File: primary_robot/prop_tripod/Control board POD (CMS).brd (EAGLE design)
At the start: 100.7 x 157 mm, 94 parts, among them IC3 NE555D, Q1 MOSFET-NCHANNELD2PAK, Q2 MOSFET-NCHANNELD2PAK, Q3 MOSFET-NCHANNELD2PAK, Q4 MOSFET-NCHANNELD2PAK

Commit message: [prop_tripod] Updates to pre-Rev2
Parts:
- removed C10: 120nF, resistor:A/3216-18W
- removed C9: 330nF, rcl:A/3216-18R
- removed MC78M05ABT: MC78M05ABDT, linear:DPACK_3
- added R17: 1k, SparkFun-Passives:0603-RES
- moved R40 9.27 mm to (10.8, 124.5)
- moved D14 7.23 mm to (12.1, 97.8)
- moved C4 7.08 mm to (17.6, 100.2)
- moved D7 6.49 mm to (14.5, 101.0)
- moved LED1 5.74 mm to (-14.1, 104.1)
- moved Q1 5.72 mm to (-5.35, 104.1)
- moved Q2 5.72 mm to (-5.35, 131.0)
- moved R1 5.21 mm to (-14.1, 96.5)
- moved C7 4.59 mm to (-15.7, 113.0)
- moved BAT 4.57 mm to (-21.6, 100.3)
- moved TPS2 4.57 mm to (-16.6, 136.1)
- moved C8 3.70 mm to (-20.1, 111.3)
- moved C1 3.69 mm to (-21.8, 119.3)
- moved R41 3.68 mm to (13.1, 108.3), turned to 270 degrees
- moved M 3.05 mm to (-21.5, 126.4)
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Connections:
- removed net 5V_PWR: C10.+, MC78M05ABT.3
- net 12V_BAT: now also R17.2, TPS1.C; no longer C9.+, MC78M05ABT.1, TPS1.A
- net GND_PWR: now also TPS1.A, TPS2.A, TPS3.A; no longer C10.-, C9.-, MC78M05ABT.4, TPS1.C, TPS2.C, TPS3.C
- net N$11: now also TPS2.C; no longer TPS2.A
- net N$3: now also TPS3.C; no longer TPS3.A
- net N$64: now also R17.1
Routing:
- net N$3: track 98.5 -> 131.3 mm
- net 5V_PWR: track 10.5 -> 0.00 mm
- net 12V_BAT: track 316.1 -> 306.3 mm, vias 4 -> 5
- net GATE_Q3: track 23.2 -> 15.1 mm
- net N$2: track 66.3 -> 58.4 mm
- net N$11: track 71.8 -> 78.2 mm
- net GND_CMD: track 306.9 -> 312.9 mm
- net BSTRP: track 61.9 -> 56.2 mm
- net N$64: track 15.8 -> 18.7 mm
- net GND_PWR: track 445.4 -> 442.5 mm, vias 9 -> 10
- net DIR_POD3_LPC: track 14.2 -> 16.7 mm
- net DIR_POD1_LPC: track 11.5 -> 14.0 mm
- net PWM_POD2_LPC: track 14.8 -> 17.3 mm
- net PWM_POD1_LPC: track 11.2 -> 13.8 mm
- net PWM_POD3_LPC: track 16.0 -> 18.6 mm
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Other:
- board text added: "Carte POD rev2"
- board text removed: "Carte POD rev1"

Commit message: [prop-tripod] Update the footprint of the LPC, increase the readability of some name on the board
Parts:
- moved CON_POD2 2.54 mm to (-34.2, 24.4)
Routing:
- net GND_CMD: track 312.9 -> 316.6 mm
- net 3V3: track 46.2 -> 49.9 mm
- net DIR_POD2__LPC: track 38.6 -> 41.2 mm
- net PWM_POD2__LPC: track 32.0 -> 34.5 mm
- net RX0_LPC: track 16.9 -> 15.2 mm

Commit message: [prop_tripod] Fixes RST connection
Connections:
- net GND_CMD: no longer EXT2.26
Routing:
- net GND_CMD: track 316.6 -> 317.9 mm
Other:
- board text added: "3V3"
- board text removed: "3V"
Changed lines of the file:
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@@
 <text x="-38.735" y="30.5308" size="1.6764" layer="1" font="vector" ratio="20" rot="R270">POD2</text>
 <text x="-38.989" y="11.1252" size="1.6764" layer="1" font="vector" ratio="20" rot="R180">5V</text>
-<text x="-32.6898" y="14.2748" size="1.6764" layer="1" font="vector" ratio="20" rot="R180">3V</text>
+<text x="-31.4198" y="14.2748" size="1.6764" layer="1" font="vector" ratio="20" rot="R180">3V3</text>
 <text x="32.4292" y="14.732" size="1.6764" layer="1" font="vector" ratio="20" rot="R270">ENC3</text>
 <text x="32.1752" y="31.369" size="1.6764" layer="1" font="vector" ratio="20" rot="R270">ENC2</text>
@@
 <contactref element="EXT1" pad="26"/>
 <contactref element="EXT2" pad="25"/>
-<contactref element="EXT2" pad="26"/>
 <contactref element="COD_POD2" pad="5"/>
 <contactref element="COD_POD3" pad="5"/>
 <wire x1="-35.4076" y1="5.0546" x2="-32.3596" y2="8.1026" width="0.8128" layer="16"/>
-<wire x1="-24.257" y1="10.414" x2="-24.2316" y2="10.4394" width="0.8128" layer="16"/>
-<wire x1="-24.2316" y1="10.4394" x2="-21.6916" y2="10.4394" width="0.8128" layer="16"/>
 <wire x1="-34.368221875" y1="36.3196" x2="-34.3675" y2="33.7785" width="0.8128" layer="16"/>
 <wire x1="-35.7645" y1="5.4115" x2="-35.4076" y2="5.0546" width="0.8128" layer="16"/>
@@
 <wire x1="15.7226" y1="54.2036" x2="13.4808" y2="51.4858" width="0.8128" layer="1"/>
 <wire x1="-32.3596" y1="8.1026" x2="-31.467" y2="10.417" width="0.8128" layer="16"/>
-<wire x1="-31.467" y1="10.417" x2="-24.2316" y2="10.4394" width="0.8128" layer="16"/>
 <wire x1="14.1732" y1="59.0042" x2="14.1732" y2="55.3212" width="0.8128" layer="16"/>
 <wire x1="14.1732" y1="55.3212" x2="15.7226" y2="54.2036" width="0.8128" layer="16"/>
 <wire x1="-7.206" y1="38.2143" x2="-7.1882" y2="39.0144" width="0.3048" layer="16"/>
-<wire x1="-32.8676" y1="24.4094" x2="-37.7444" y2="25.9334" width="0.8128" layer="16"/>
+<wire x1="-35.4076" y1="24.4094" x2="-37.7444" y2="25.9334" width="0.8128" layer="16"/>
 <wire x1="-37.7444" y1="25.9334" x2="-37.7444" y2="30.6578" width="0.8128" layer="16"/>
 <wire x1="-37.7444" y1="30.6578" x2="-34.3675" y2="33.7785" width="0.8128" layer="16"/>
@@
 <via x="-1.7272" y="10.3632" extent="1-16" drill="0.6" diameter="1.6764"/>
 <wire x1="-1.7272" y1="10.3632" x2="-14.0462" y2="10.3886" width="0.8128" layer="1"/>
-<wire x1="-34.1798" y1="24.4314" x2="-32.8676" y2="24.4094" width="0.6096" layer="16"/>
+<wire x1="-34.1798" y1="24.4314" x2="-35.4076" y2="24.4094" width="0.6096" layer="16"/>
 <wire x1="15.7226" y1="54.2036" x2="20.8026" y2="54.2036" width="0.8128" layer="1"/>
 <via x="20.8026" y="54.2036" extent="1-16" drill="0.6" diameter="1.6764"/>
@@
 <wire x1="-31.9024" y1="46.5328" x2="-27.5021" y2="46.5356" width="0.8128" layer="16"/>
 <wire x1="-27.5021" y1="46.5356" x2="-27.5082" y2="49.784" width="0.8128" layer="16"/>
+<wire x1="-21.6916" y1="10.4394" x2="-21.59" y2="10.4394" width="0.4064" layer="16"/>
+<wire x1="-21.59" y1="10.4394" x2="-21.59" y2="8.89" width="0.8128" layer="16"/>
+<wire x1="-21.59" y1="8.89" x2="-22.86" y2="7.62" width="0.8128" layer="16"/>
+<wire x1="-22.86" y1="7.62" x2="-29.21" y2="7.62" width="0.8128" layer="16"/>
+<wire x1="-29.21" y1="7.62" x2="-31.467" y2="9.877" width="0.8128" layer="16"/>
+<wire x1="-31.467" y1="9.877" x2="-31.467" y2="10.417" width="0.8128" layer="16"/>
 </signal>
 <signal name="GND_PWR">

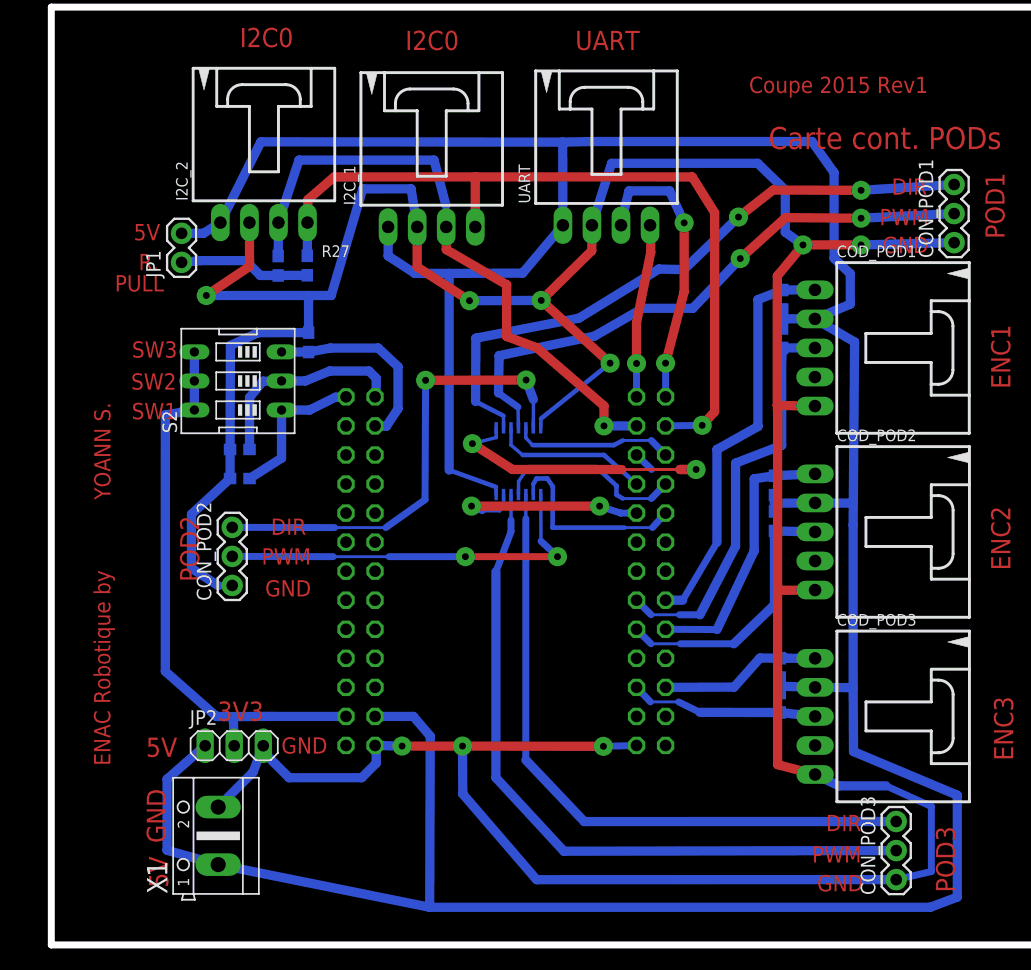
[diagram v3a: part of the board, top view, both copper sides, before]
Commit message: [prop_tripod] Fixes buffer pull-ups + I²C pull-ups headers
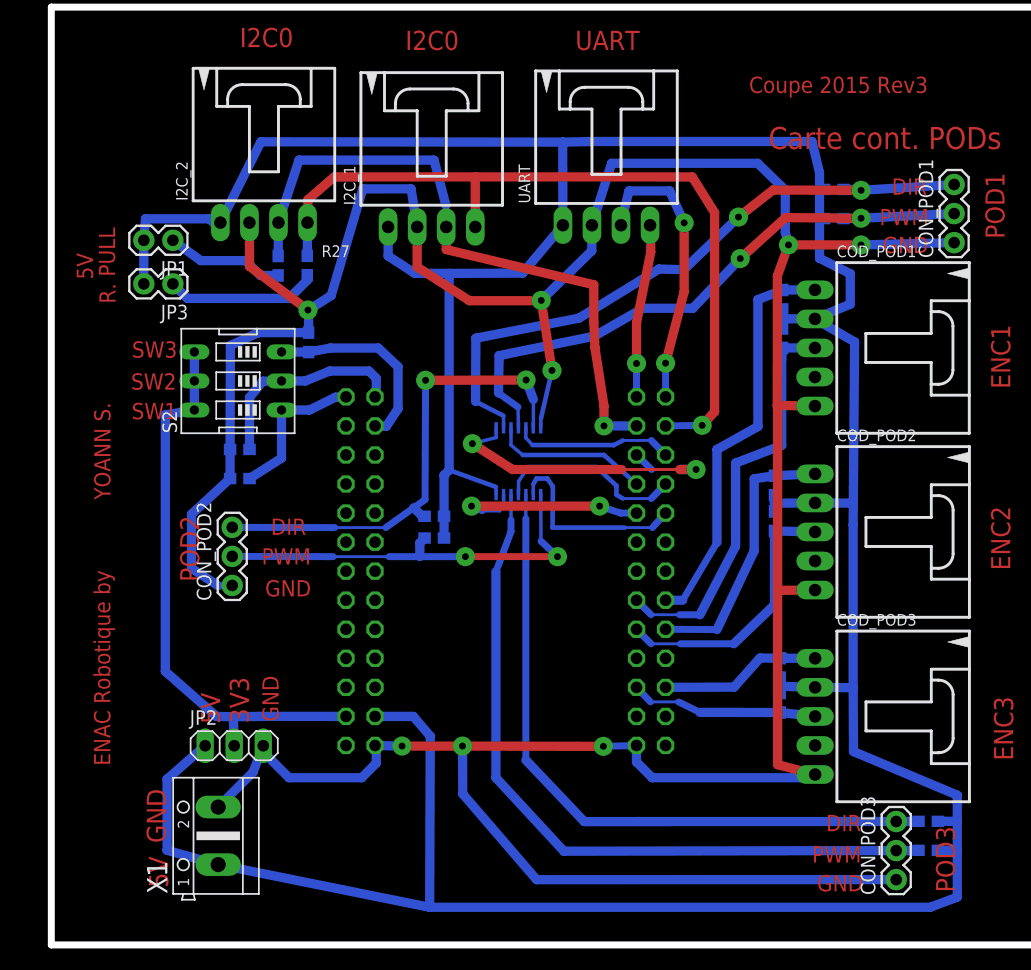
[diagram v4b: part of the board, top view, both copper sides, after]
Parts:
- added JP3: (no value), SparkFun:1X02
- added R18, R19, R20, R22, R23, R24: 3.3k, SparkFun-Passives:0603-RES
- moved JP1 2.08 mm to (-39.4, 54.6), turned to 180 degrees
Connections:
- new net N$54: JP3.1, R27.1
- net 5V_CMD: now also JP3.2, R18.1, R19.1, R20.1, R22.1, R23.1, R24.1
- net DIR_POD1_LPC: now also EXT1.6, U2.1; no longer EXT1.5, U2.5
- net DIR_POD1__LPC: now also R18.2
- net DIR_POD2_LPC: now also EXT1.5, U2.5; no longer EXT1.6, U2.1
- net DIR_POD2__LPC: now also R22.2
- net DIR_POD3__LPC: now also R24.2
- net N$52: no longer R27.1
- net PWM_POD1__LPC: now also R19.2
- net PWM_POD2__LPC: now also R20.2
- net PWM_POD3__LPC: now also R23.2
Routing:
- net 5V_CMD: track 308.4 -> 328.3 mm
- net GND_CMD: track 317.9 -> 302.6 mm, vias 9 -> 8
- net DIR_POD2_LPC: track 28.9 -> 14.0 mm, vias 2 -> 0
- net DIR_POD1_LPC: track 14.0 -> 28.9 mm, vias 0 -> 2
- net N$54: track 0.00 -> 13.4 mm
- net SDA0_LPC: track 54.3 -> 57.0 mm
- net PWM_POD3__LPC: track 62.8 -> 64.8 mm
- net DIR_POD3__LPC: track 57.9 -> 59.9 mm
- net PWM_POD2__LPC: track 34.5 -> 36.3 mm
- net DIR_POD1__LPC: track 55.2 -> 56.8 mm
- net PWM_POD1__LPC: track 51.0 -> 52.6 mm
- net DIR_POD2__LPC: track 41.2 -> 42.4 mm
- net N$52: track 11.5 -> 10.3 mm
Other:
- board text added: "Coupe 2015 Rev3"
- board text removed: "Coupe 2015 Rev1"

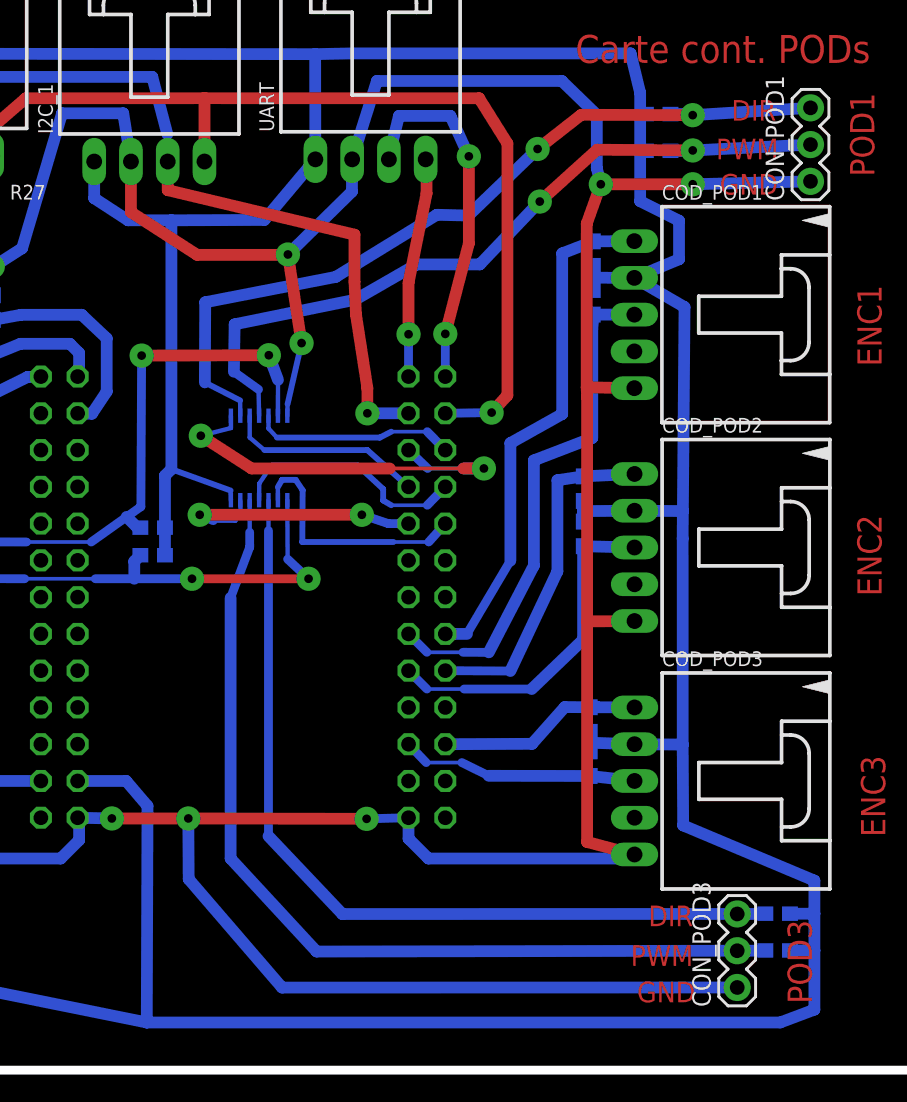
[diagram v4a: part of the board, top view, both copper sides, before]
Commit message: [prop_tripod] Removes useless buffer
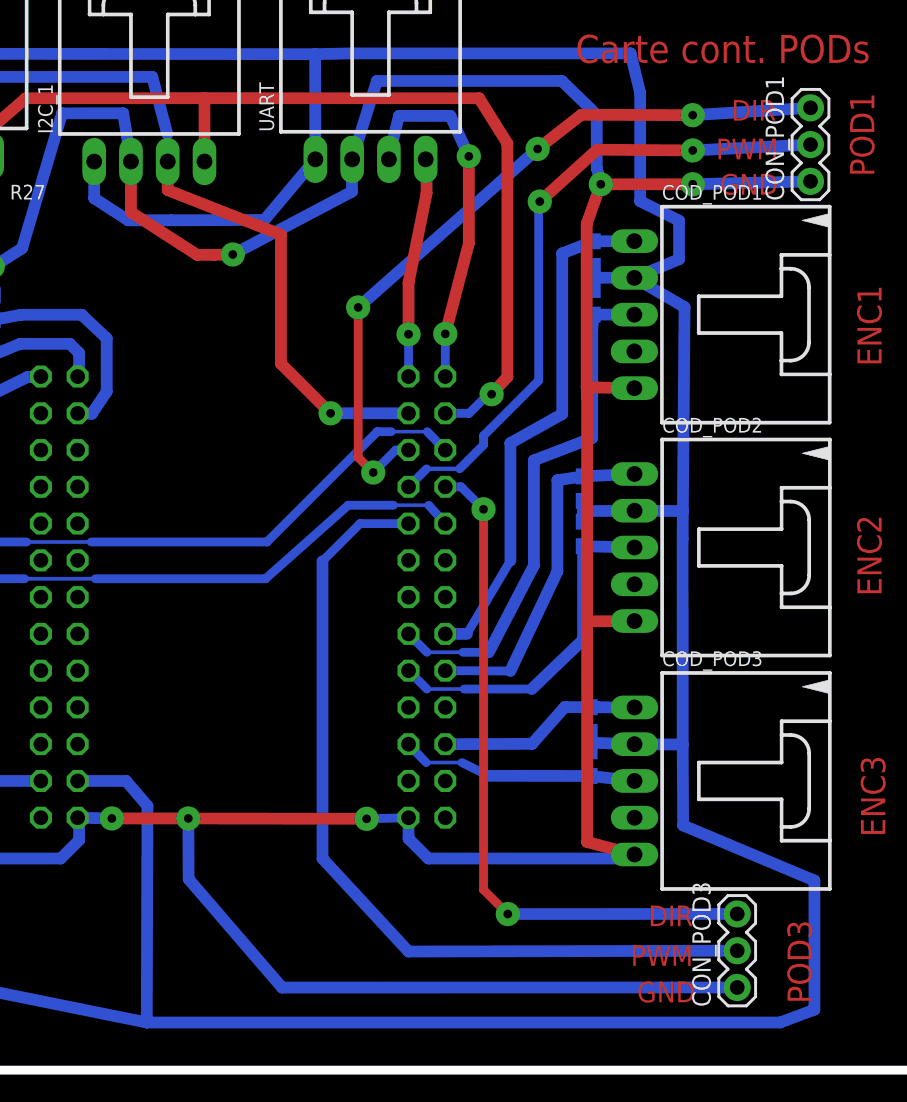
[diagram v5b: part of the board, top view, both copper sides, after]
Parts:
- removed R18, R19, R20, R22, R23, R24: 3.3k, SparkFun-Passives:0603-RES
- removed U2: (no value), SparkFun-DigitalIC:TSSOP14
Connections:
- removed net DIR_POD1__LPC: CON_POD1.3, R18.2, U2.2
- removed net DIR_POD2__LPC: CON_POD2.3, R22.2, U2.6
- removed net DIR_POD3__LPC: CON_POD3.3, R24.2, U2.10
- removed net PWM_POD1__LPC: CON_POD1.2, R19.2, U2.4
- removed net PWM_POD2__LPC: CON_POD2.2, R20.2, U2.8
- removed net PWM_POD3__LPC: CON_POD3.2, R23.2, U2.12
- net 5V_CMD: no longer R18.1, R19.1, R20.1, R22.1, R23.1, R24.1, U2.14
- net DIR_POD1_LPC: now also CON_POD1.3; no longer U2.1
- net DIR_POD2_LPC: now also CON_POD2.3; no longer U2.5
- net DIR_POD3_LPC: now also CON_POD3.3; no longer U2.11
- net GND_CMD: no longer U2.7
- net PWM_POD1_LPC: now also CON_POD1.2; no longer U2.3
- net PWM_POD2_LPC: now also CON_POD2.2; no longer U2.9
- net PWM_POD3_LPC: now also CON_POD3.2; no longer U2.13
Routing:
- net PWM_POD3__LPC: track 64.8 -> 0.00 mm
- net DIR_POD3__LPC: track 59.9 -> 0.00 mm
- net DIR_POD1__LPC: track 56.8 -> 0.00 mm, vias 2 -> 0
- net PWM_POD1__LPC: track 52.6 -> 0.00 mm, vias 2 -> 0
- net DIR_POD2__LPC: track 42.4 -> 0.00 mm, vias 2 -> 0
- net PWM_POD3_LPC: track 18.6 -> 59.0 mm, vias 2 -> 0
- net PWM_POD2__LPC: track 36.3 -> 0.00 mm, vias 2 -> 0
- net 5V_CMD: track 328.3 -> 295.8 mm
- net PWM_POD1_LPC: track 13.8 -> 45.4 mm, vias 0 -> 2
- net DIR_POD3_LPC: track 16.7 -> 47.8 mm, vias 0 -> 2
- net DIR_POD2_LPC: track 14.0 -> 41.6 mm
- net PWM_POD2_LPC: track 17.3 -> 40.4 mm
- net DIR_POD1_LPC: track 28.9 -> 51.2 mm, vias 2 -> 4
- net GND_CMD: track 302.6 -> 290.6 mm, vias 8 -> 7
- net SDA0_LPC: track 57.0 -> 56.0 mm
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
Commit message: [prop_tripod] Changes pin asssignation
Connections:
- removed net SD2_POD3_LPC: EXT1.13
- net CHA_POD1_LPC: now also EXT1.13; no longer EXT1.16
- net CHB_POD1_LPC: now also EXT1.16; no longer EXT1.15
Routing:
- net CHA_POD1_LPC: track 35.8 -> 29.7 mm
- net CHB_POD1_LPC: track 35.8 -> 38.3 mm
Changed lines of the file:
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@@
 <contactref element="R21" pad="1"/>
 <contactref element="COD_POD1" pad="1"/>
-<contactref element="EXT1" pad="15"/>
 <wire x1="16.7707" y1="50.276" x2="13.9525" y2="50.2625" width="0.8128" layer="16"/>
-<wire x1="3.7084" y1="23.1394" x2="5.207" y2="23.1394" width="0.8128" layer="16"/>
-<wire x1="8.2042" y1="28.194" x2="8.2042" y2="36.322" width="0.8128" layer="16"/>
+<wire x1="8.2042" y1="29.464" x2="8.2042" y2="36.322" width="0.8128" layer="16"/>
 <wire x1="8.2042" y1="36.322" x2="11.7856" y2="38.3286" width="0.8128" layer="16"/>
 <wire x1="11.7856" y1="38.3286" x2="11.7856" y2="49.4284" width="0.8128" layer="16"/>
 <wire x1="11.7856" y1="49.4284" x2="13.9525" y2="50.2625" width="0.8128" layer="16"/>
-<wire x1="5.207" y1="23.1394" x2="8.2042" y2="28.194" width="0.6096" layer="16"/>
+<wire x1="5.207" y1="26.9494" x2="8.2042" y2="29.464" width="0.6096" layer="16"/>
+<contactref element="EXT1" pad="16"/>
+<wire x1="5.207" y1="26.9494" x2="2.54" y2="26.9494" width="0.254" layer="16"/>
+<wire x1="2.54" y1="26.9494" x2="2.54" y2="24.13" width="0.254" layer="16"/>
+<wire x1="2.54" y1="24.13" x2="1.1684" y2="23.1394" width="0.6096" layer="16"/>
 </signal>
 <signal name="CHB_POD2_LPC">
@@
 <wire x1="-2.9972" y1="32.0294" x2="-8.7122" y2="26.9494" width="0.6096" layer="16"/>
 </signal>
-<signal name="SD2_POD3_LPC">
-<contactref element="EXT1" pad="13"/>
-</signal>
 <signal name="CHA_POD1_LPC">
 <contactref element="COD_POD1" pad="3"/>
 <contactref element="R25" pad="2"/>
-<contactref element="EXT1" pad="16"/>
-<wire x1="1.1684" y1="23.1394" x2="2.4384" y2="21.8694" width="0.6096" layer="16"/>
-<wire x1="2.4384" y1="21.8694" x2="4.9276" y2="21.8694" width="0.254" layer="16"/>
 <wire x1="13.9474" y1="45.1996" x2="16.7707" y2="45.196" width="0.8128" layer="16"/>
-<wire x1="6.7128375" y1="21.86285625" x2="9.8298" y2="27.8638" width="0.8128" layer="16"/>
+<wire x1="6.7128375" y1="25.67285625" x2="9.8298" y2="27.8638" width="0.8128" layer="16"/>
 <wire x1="9.8298" y1="27.8638" x2="9.8298" y2="35.1282" width="0.8128" layer="16"/>
 <wire x1="9.8298" y1="35.1282" x2="13.8618" y2="36.6776" width="0.8128" layer="16"/>
 <wire x1="13.8618" y1="36.6776" x2="13.8618" y2="44.1706" width="0.8128" layer="16"/>
 <wire x1="13.8618" y1="44.1706" x2="13.9474" y2="45.1996" width="0.8128" layer="16"/>
-<wire x1="4.9276" y1="21.8694" x2="6.7128375" y2="21.86285625" width="0.6096" layer="16"/>
+<contactref element="EXT1" pad="13"/>
+<wire x1="6.7128375" y1="25.67285625" x2="3.7084" y2="25.6794" width="0.6096" layer="16"/>
 </signal>
 <signal name="CHA_POD2_LPC">
